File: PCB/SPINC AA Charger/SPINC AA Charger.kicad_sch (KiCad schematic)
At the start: 100 parts, among them J1 USB_C_Receptacle_USB2.0, J2 Conn_01x03_Pin, J3 Conn_01x10_Socket, J4 Conn_01x01_Pin, J5 Conn_01x01_Pin, Q1 DMG2301L, Q2 DMHC3025LSD, Q3 DMG2301L, Q4 DMG2301L, Q5 SI2305CDS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

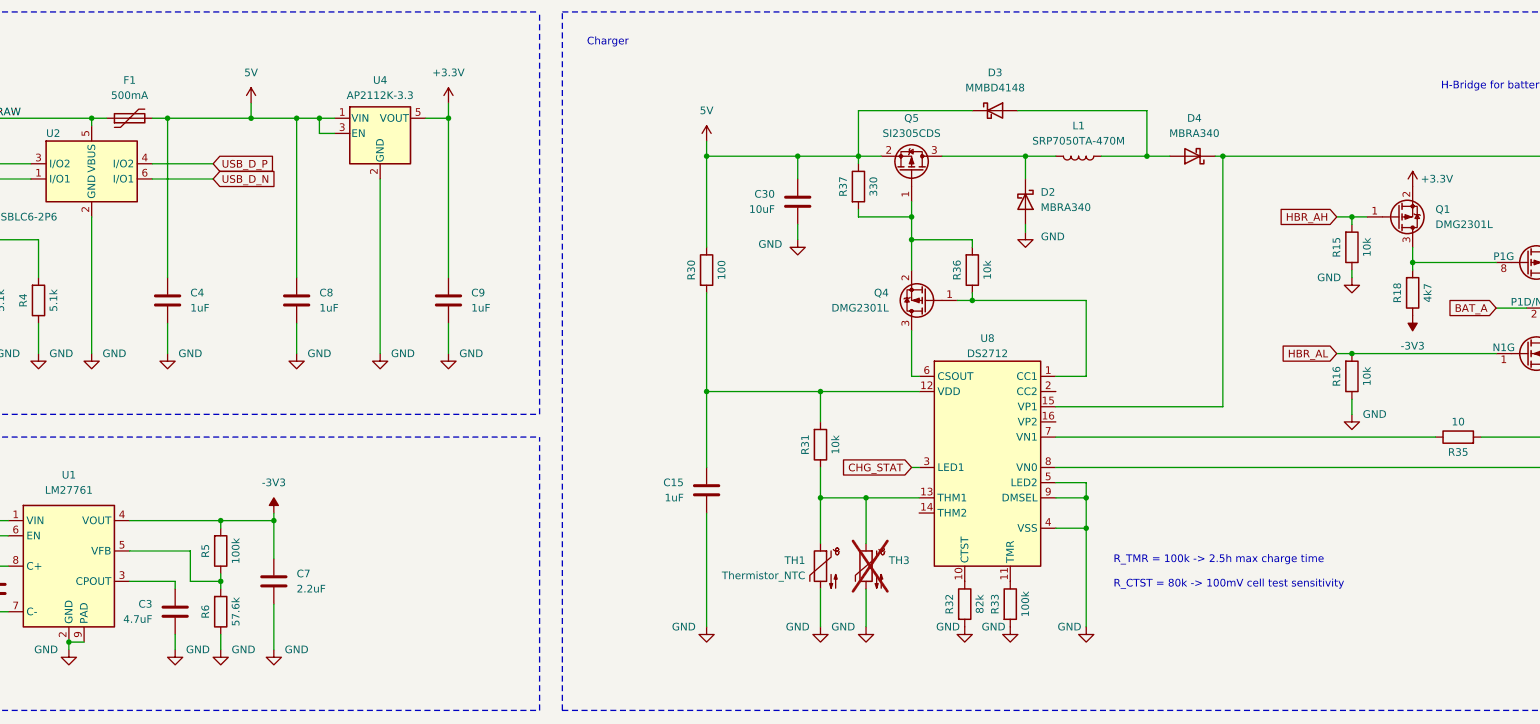
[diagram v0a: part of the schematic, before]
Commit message: Small fixes for the PCB
- Changed fuse from 500mA to 1A (when charging at full 1A, the device draws slightly more than 500mA)
- Changed R32 from 80k to 22k (somehow the cell check fails with 100mV sensitivity)
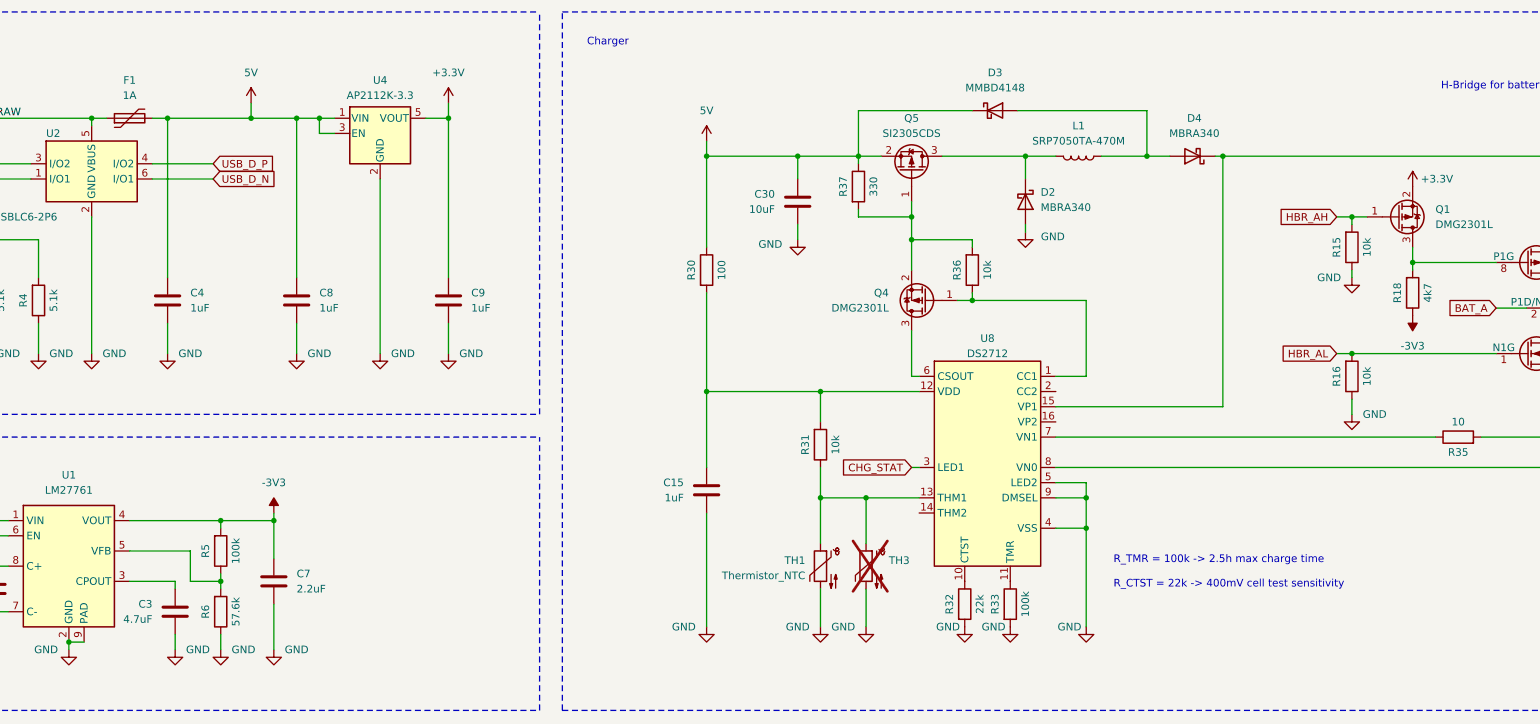
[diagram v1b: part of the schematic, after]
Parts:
- F1: value 500mA -> 1A
- R32: value 82k -> 22k
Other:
- note added: "R_TMR = 100k -> 2.5h max charge time R_CTST = 22k -> 400mV cell test sensitivity"
- note removed: "R_TMR = 100k -> 2.5h max charge time R_CTST = 80k -> 100mV cell test sensitivity"
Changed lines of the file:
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@@
 		)
 	)
-	(text "R_TMR = 100k -> 2.5h max charge time\n\nR_CTST = 80k -> 100mV cell test sensitivity"
+	(text "R_TMR = 100k -> 2.5h max charge time\n\nR_CTST = 22k -> 400mV cell test sensitivity"
 		(exclude_from_sim no)
 		(at 250.952 108.966 0)
@@
 			)
 		)
-		(property "Value" "82k"
+		(property "Value" "22k"
 			(at 228.6 114.3 90)
 			(effects
@@
 			)
 		)
-		(property "Value" "500mA"
+		(property "Value" "1A"
 			(at 86.36 29.21 90)
 			(effects

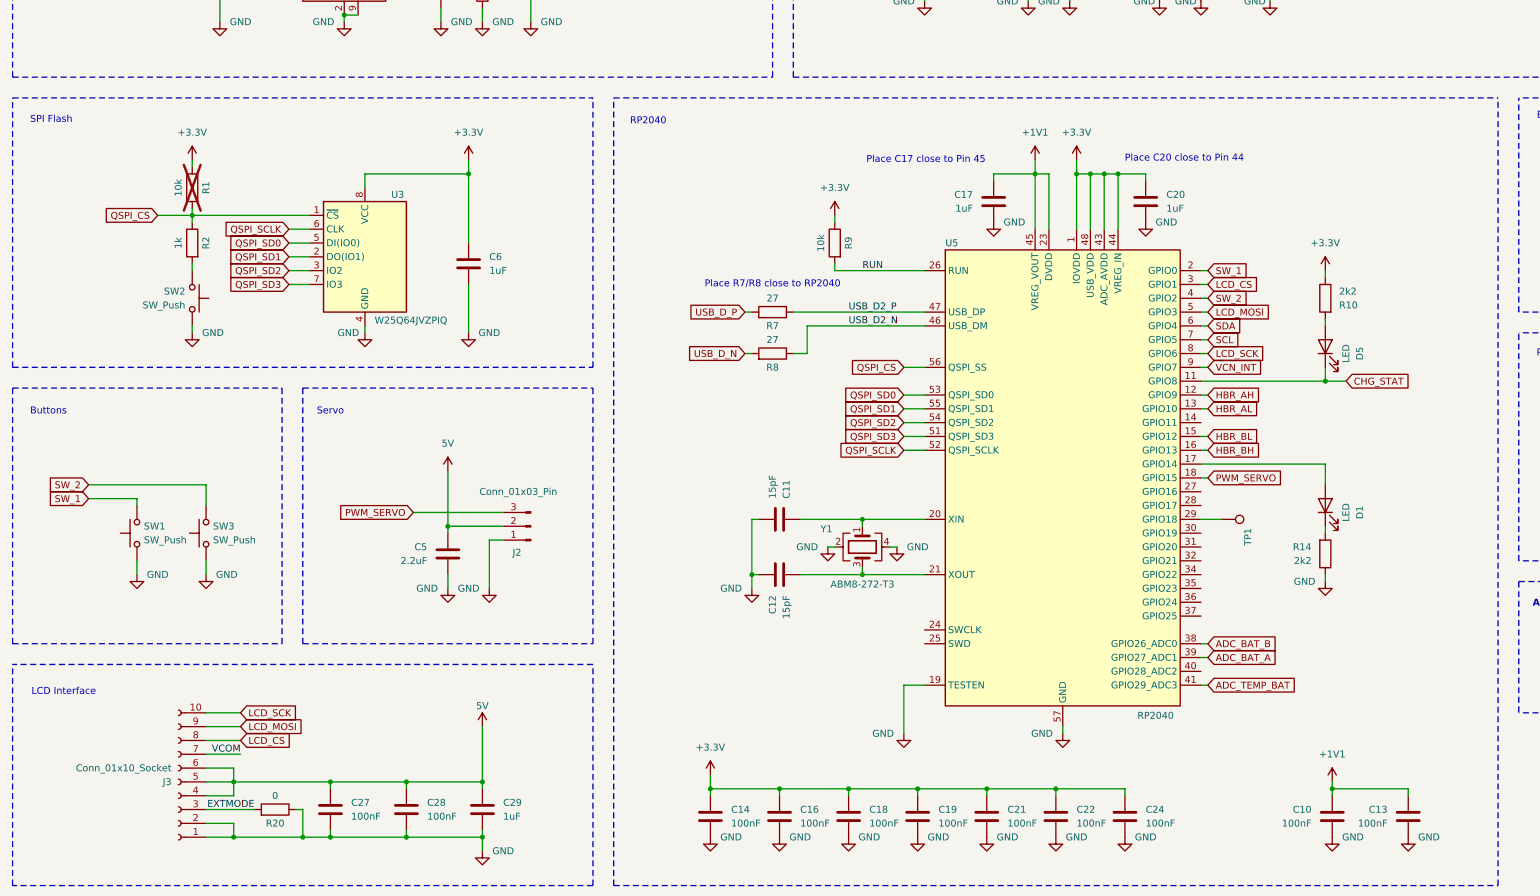
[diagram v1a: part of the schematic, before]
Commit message: Add ESP32-WROOM-32U and CH340 instead of RP2040
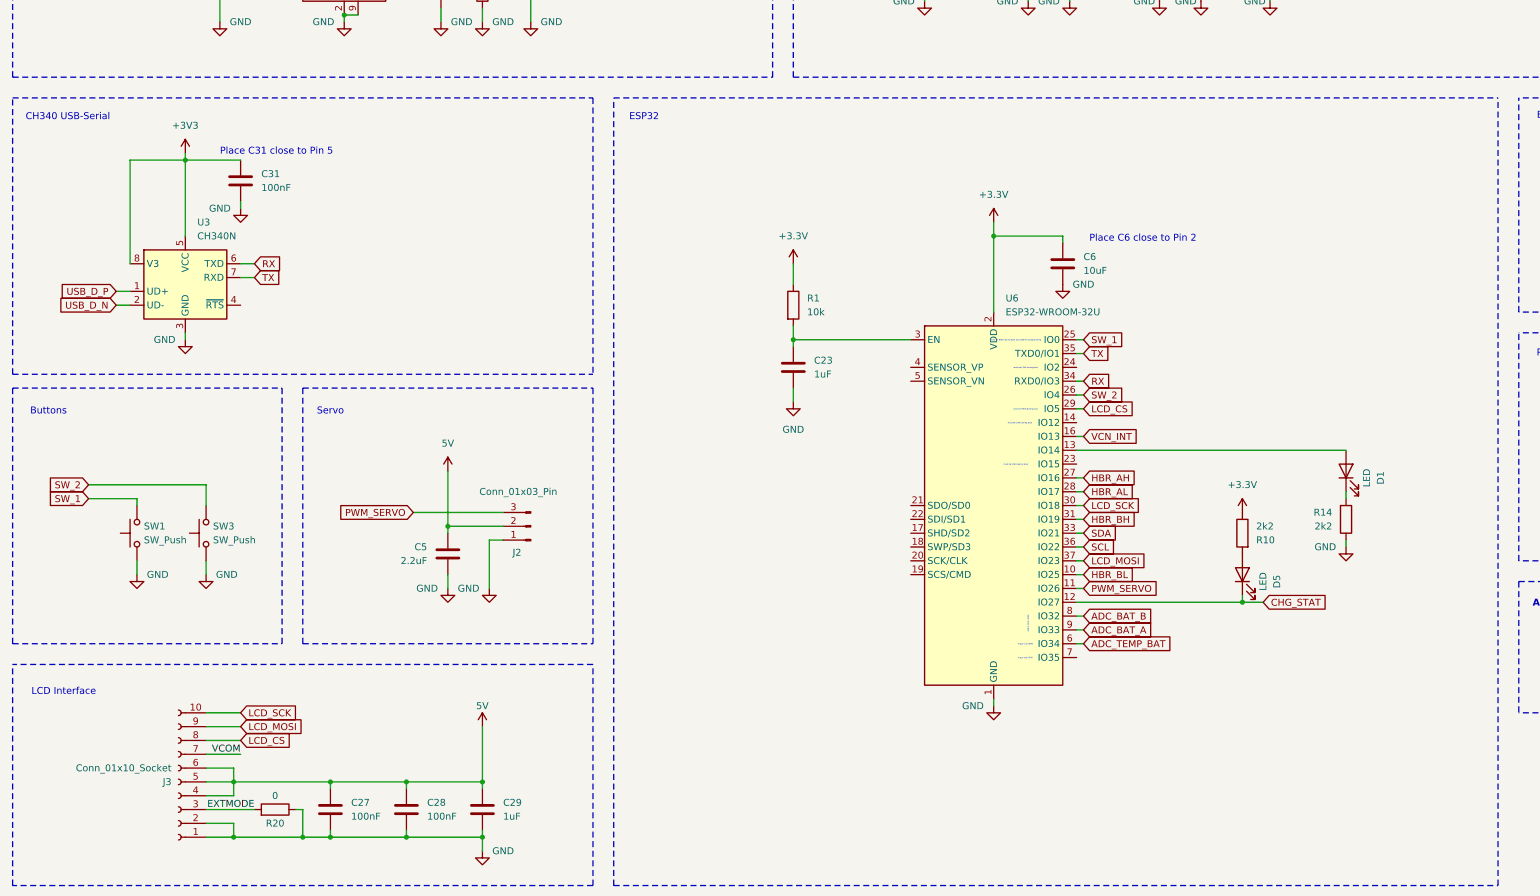
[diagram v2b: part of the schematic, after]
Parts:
- removed C10, C13, C14, C16, C18, C19, C21, C22, C24: 100nF, Capacitor_SMD:C_0603_1608Metric, symbol Device:C
- removed C11, C12: 15pF, Capacitor_SMD:C_0603_1608Metric, symbol Device:C
- removed C17, C20: 1uF, Capacitor_SMD:C_0603_1608Metric, symbol Device:C
- removed R2: 1k, Resistor_SMD:R_0603_1608Metric, symbol Device:R
- removed R7, R8: 27, Resistor_SMD:R_0603_1608Metric, symbol Device:R
- removed R9: 10k, Resistor_SMD:R_0603_1608Metric, symbol Device:R
- removed SW2: SW_Push, Button_Switch_SMD:SW_SPST_EVQP2, symbol Switch:SW_Push
- removed TP1: TestPoint, TestPoint:TestPoint_Pad_D1.5mm, symbol Connector:TestPoint
- removed U3: W25Q64JVZPIQ, Package_SON:WSON-8-1EP_6x5mm_P1.27mm_EP3.4x4.3mm, symbol Memory_Flash:W25Q128JVS
- removed U5: RP2040, Package_DFN_QFN:QFN-56-1EP_7x7mm_P0.4mm_EP3.2x3.2mm, symbol MCU_RaspberryPi:RP2040
- removed Y1: ABM8-272-T3, Crystal:Crystal_SMD_Abracon_ABM8G-4Pin_3.2x2.5mm, symbol Device:Crystal_GND24
- added C23: 1uF, symbol Device:C
- added C31: 100nF, symbol Device:C
- added U3: CH340N, Package_SO:SOP-8_3.9x4.9mm_P1.27mm, symbol Interface_USB:CH340N
- added U6: ESP32-WROOM-32U, RF_Module:ESP32-WROOM-32U, symbol RF_Module:ESP32-WROOM-32U
- C6: value 1uF -> 10uF
- R1: footprint Resistor_SMD:R_0603_1608Metric -> (none); now fitted; now in the parts list
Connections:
- net +3.3V: now also U6.2 (VDD)
- net ADC_BAT_A: now also U6.9 (IO33)
- net ADC_BAT_B: now also U6.8 (IO32)
- net ADC_TEMP_BAT: now also U6.6 (IO34)
- net CHG_STAT: now also U6.12 (IO27)
- net GND: now also C23.2, C31.2, U3.3 (GND), U6.1 (GND), U6.15 (GND), U6.38 (GND), U6.39 (GND)
- net HBR_AH: now also U6.27 (IO16)
- net HBR_AL: now also U6.28 (IO17)
- net HBR_BH: now also U6.31 (IO19)
- net HBR_BL: now also U6.10 (IO25)
- net LCD_CS: now also U6.29 (IO5)
- net LCD_MOSI: now also U6.37 (IO23)
- net LCD_SCK: now also U6.30 (IO18)
- net PWM_SERVO: now also U6.11 (IO26)
- net SCL: now also U6.36 (IO22)
- net SDA: now also U6.33 (IO21)
- net SW_1: now also U6.25 (IO0)
- net SW_2: now also U6.26 (IO4)
- net USB_D_N: now also U3.2 (UD-)
- net USB_D_P: now also U3.1 (UD+)
- net VCN_INT: now also U6.16 (IO13)
- net at D1.2 (A): now also U6.13 (IO14)
- net QSPI_CS: no longer names the net of R1.2
- net QSPI_CS: now also C23.1, U6.3 (EN)
- new net +3V3: C31.1, U3.5 (VCC), U3.8 (V3)
- new net RX: U3.6 (TXD), U6.34 (RXD0/IO3)
- new net TX: U3.7 (RXD), U6.35 (TXD0/IO1)
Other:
- note added: "ADC1: IO32--IO39"
- note added: "CH340 USB-Serial"
- note added: "ESP32"
- note added: "Input only GPIO"
- note added: "Place C31 close to Pin 5"
- note added: "Place C6 close to Pin 2"
- note added: "must be HIGH during boot"
- note added: "must be HIGH during boot and LOW for programming"
- note added: "must be LOW during boot"
- note removed: "Place C17 close to Pin 45"
- note removed: "Place C20 close to Pin 44"
- note removed: "Place R7/R8 close to RP2040"
- note removed: "RP2040"
- note removed: "SPI Flash"

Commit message: WIP: initial pcb placement
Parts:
- C23, C31: footprint (none) -> Capacitor_SMD:C_0603_1608Metric
- R1: footprint (none) -> Resistor_SMD:R_0603_1608Metric
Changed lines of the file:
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@@
 			)
 		)
-		(property "Footprint" ""
+		(property "Footprint" "Capacitor_SMD:C_0603_1608Metric"
 			(at 58.1152 154.94 0)
 			(effects
@@
 			)
 		)
-		(property "Footprint" ""
+		(property "Footprint" "Resistor_SMD:R_0603_1608Metric"
 			(at 156.972 173.99 90)
 			(effects
@@
 			)
 		)
-		(property "Footprint" ""
+		(property "Footprint" "Capacitor_SMD:C_0603_1608Metric"
 			(at 159.7152 189.23 0)
 			(effects

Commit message: Fabrication details
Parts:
- C23, C29: LCSC (none) -> C15849
- J2: LCSC (none) -> C722693
- R10, R14: LCSC C114662 -> C4190
- R3, R4: LCSC C114626 -> C23186
- R5: LCSC C114626 -> C25803
- R6: LCSC C114626 -> C170635
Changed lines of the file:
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@@
 			)
 		)
+		(property "LCSC" "C722693"
+			(at 110.49 214.63 0)
+			(effects
+				(font
+					(size 1.27 1.27)
+				)
+				(hide yes)
+			)
+		)
 		(pin "2"
 		)
@@
 			)
 		)
-		(property "LCSC" "C114626"
+		(property "LCSC" "C23186"
 			(at 71.12 63.5 0)
 			(effects
@@
 			)
 		)
-		(property "LCSC" ""
+		(property "LCSC" "C15849"
 			(at 101.6 266.7 0)
 			(effects
@@
 			)
 		)
-		(property "LCSC" "C114662"
+		(property "LCSC" "C4190"
 			(at 241.3 215.9 0)
 			(effects
@@
 			)
 		)
-		(property "LCSC" "C114626"
+		(property "LCSC" "C170635"
 			(at 101.6 115.57 0)
 			(effects
@@
 			)
 		)
-		(property "LCSC" "C114626"
+		(property "LCSC" "C23186"
 			(at 62.23 63.5 0)
 			(effects
@@
 			)
 		)
-		(property "LCSC" "C114626"
+		(property "LCSC" "C25803"
 			(at 101.6 105.41 0)
 			(effects
@@
 			)
 		)
-		(property "LCSC" "C114662"
+		(property "LCSC" "C4190"
 			(at 260.35 213.36 0)
 			(effects
@@
 			(at 158.75 185.42 0)
 			(effects
+				(font
+					(size 1.27 1.27)
+				)
+				(hide yes)
+			)
+		)
+		(property "LCSC" "C15849"
+			(at 158.75 185.42 0)
+			(effects

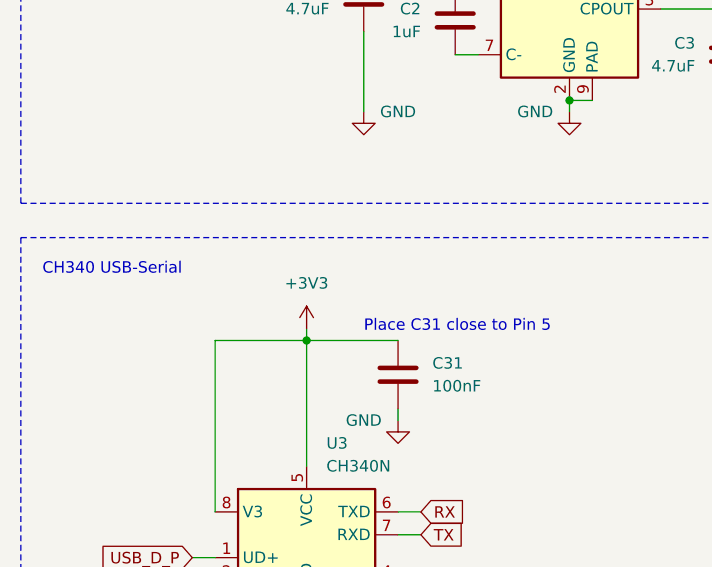
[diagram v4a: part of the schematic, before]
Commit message: Fix 3V3 supply for CH340; move capacitor to supply pin
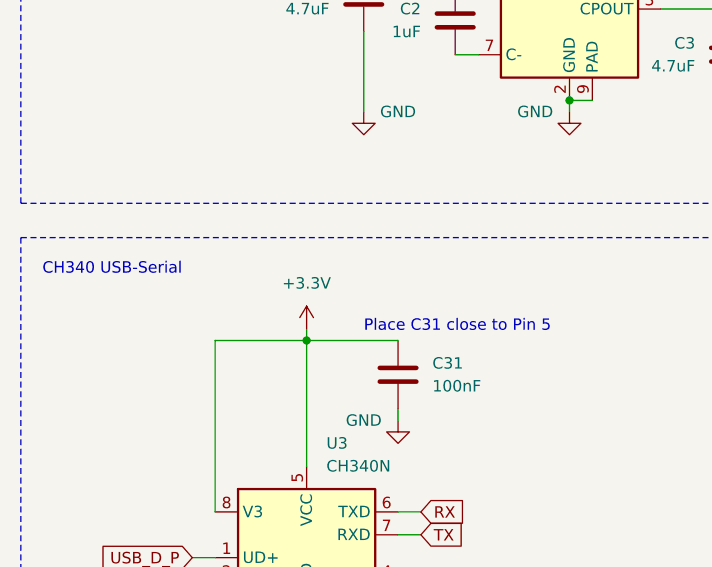
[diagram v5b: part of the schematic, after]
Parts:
- C1, C3, C30, C6, C7: LCSC C15849 -> (none)
- R5: LCSC C25803 -> (none)
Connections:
- net +3V3 is gone; now on net +3.3V: C31.1, U3.5 (VCC), U3.8 (V3)
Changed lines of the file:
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@@
 			)
 		)
-		(property "LCSC" "C15849"
+		(property "LCSC" ""
 			(at 93.98 115.57 0)
 			(effects
@@
 			)
 		)
-		(property "LCSC" "C15849"
+		(property "LCSC" ""
 			(at 53.34 109.22 0)
 			(effects
@@
 			)
 		)
-		(property "LCSC" "C15849"
+		(property "LCSC" ""
 			(at 198.12 46.99 0)
 			(effects
@@
 			)
 		)
-		(property "LCSC" "C15849"
+		(property "LCSC" ""
 			(at 110.49 110.49 0)
 			(effects
@@
 			)
 		)
-		(property "Datasheet" ""
+		(property "Datasheet" "https://www.analog.com/media/en/technical-documentation/data-sheets/DS2711-DS2712.pdf"
 			(at 229.87 96.52 0)
 			(effects
@@
 			)
 		)
-		(property "LCSC" "C25803"
+		(property "LCSC" ""
 			(at 101.6 105.41 0)
 			(effects
@@
 	)
 	(symbol
+		(lib_id "power:+3.3V")
+		(at 46.99 146.05 0)
+		(unit 1)
+		(exclude_from_sim no)
+		(in_bom yes)
+		(on_board yes)
+		(dnp no)
+		(fields_autoplaced yes)
+		(property "Reference" "#PWR018"
+			(at 46.99 149.86 0)
+			(effects
+				(font
+					(size 1.27 1.27)
+				)
+				(hide yes)
+			)
+		)
+		(property "Value" "+3.3V"
+			(at 46.99 140.97 0)
+			(effects
+				(font
+					(size 1.27 1.27)
+				)
+			)
+		)
+		(property "Footprint" ""
+			(at 46.99 146.05 0)
+			(effects
+				(font
+					(size 1.27 1.27)
+				)
+				(hide yes)
+			)
+		)
+		(property "Datasheet" ""
+			(at 46.99 146.05 0)
+			(effects
+				(font
+					(size 1.27 1.27)
+				)
+				(hide yes)
+			)
+		)
+		(property "Description" "Power symbol creates a global label with name \"+3.3V\""
+			(at 46.99 146.05 0)
+			(effects
+				(font
+					(size 1.27 1.27)
+				)
+				(hide yes)
+			)
+		)
+		(pin "1"
+		)
+		(instances
+			(project "SPINC AA Charger"
+				(path "/67a795c7-71c1-4a83-b6d2-c7272e071e9d"
+					(reference "#PWR018")
+					(unit 1)
+				)
+			)
+		)
+	)
+	(symbol
 		(lib_id "power:GND")
 		(at 114.3 72.39 0)
@@
 	)
 	(symbol
-		(lib_id "power:+3V3")
-		(at 46.99 146.05 0)
-		(unit 1)
-		(exclude_from_sim no)
-		(in_bom yes)
-		(on_board yes)
-		(dnp no)
-		(fields_autoplaced yes)
-		(property "Reference" "#PWR060"
-			(at 46.99 149.86 0)
-			(effects
-				(font
-					(size 1.27 1.27)
-				)
-				(hide yes)
-			)
-		)
-		(property "Value" "+3V3"
-			(at 46.99 140.97 0)
-			(effects
-				(font
-					(size 1.27 1.27)
-				)
-			)
-		)
-		(property "Footprint" ""
-			(at 46.99 146.05 0)
-			(effects
-				(font
-					(size 1.27 1.27)
-				)
-				(hide yes)
-			)
-		)
-		(property "Datasheet" ""
-			(at 46.99 146.05 0)
-			(effects
-				(font
-					(size 1.27 1.27)
-				)
-				(hide yes)
-			)
-		)
-		(property "Description" "Power symbol creates a global label with name \"+3V3\""
-			(at 46.99 146.05 0)
-			(effects
-				(font
-					(size 1.27 1.27)
-				)
-				(hide yes)
-			)
-		)
-		(pin "1"
-		)
-		(instances
-			(project ""
-				(path "/67a795c7-71c1-4a83-b6d2-c7272e071e9d"
-					(reference "#PWR060")
-					(unit 1)
-				)
-			)
-		)
-	)
-	(symbol
 		(lib_id "Device:R")
 		(at 260.35 213.36 0)
@@
 			)
 		)
-		(property "LCSC" "C15849"
+		(property "LCSC" ""
 			(at 208.28 166.37 0)
 			(effects
